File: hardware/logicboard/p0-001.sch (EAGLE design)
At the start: 31 parts, among them IC1 74ALS05N, IC2 LTC485N, IC3 LTC485N, J0 DC5V, J1 DIN5, J2 DIN5, J3 DIN5, X1 NELTRON-7810-XPXC, X2 NELTRON-7810-XPXC

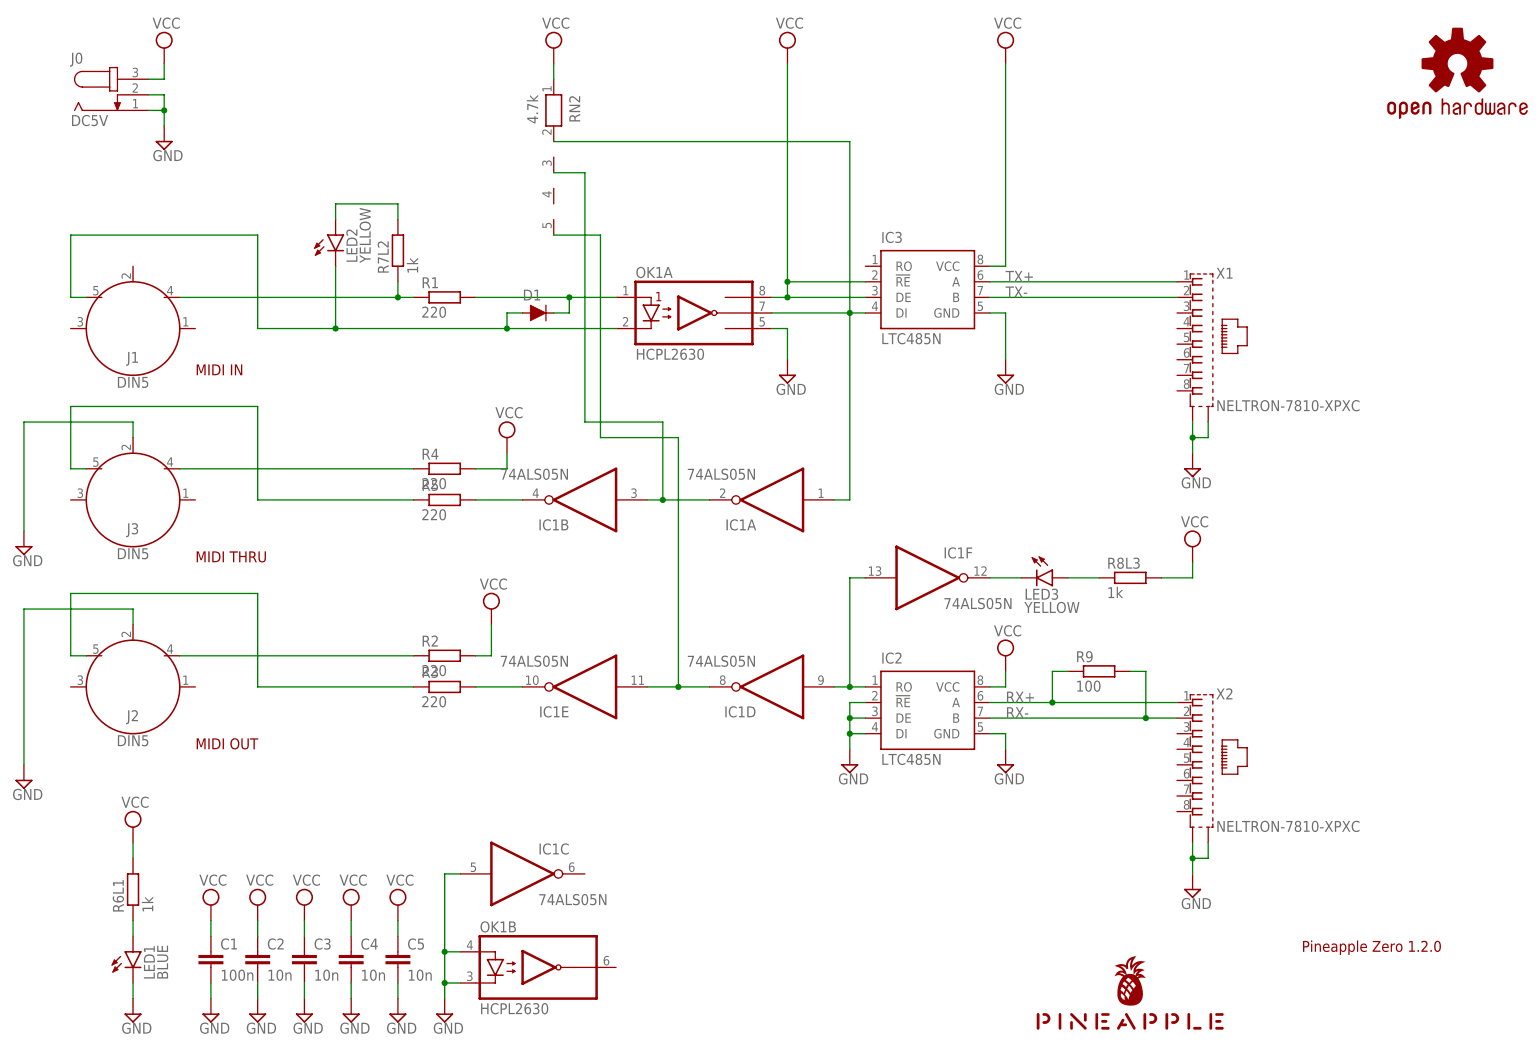
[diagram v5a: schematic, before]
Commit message: Changed led connection.
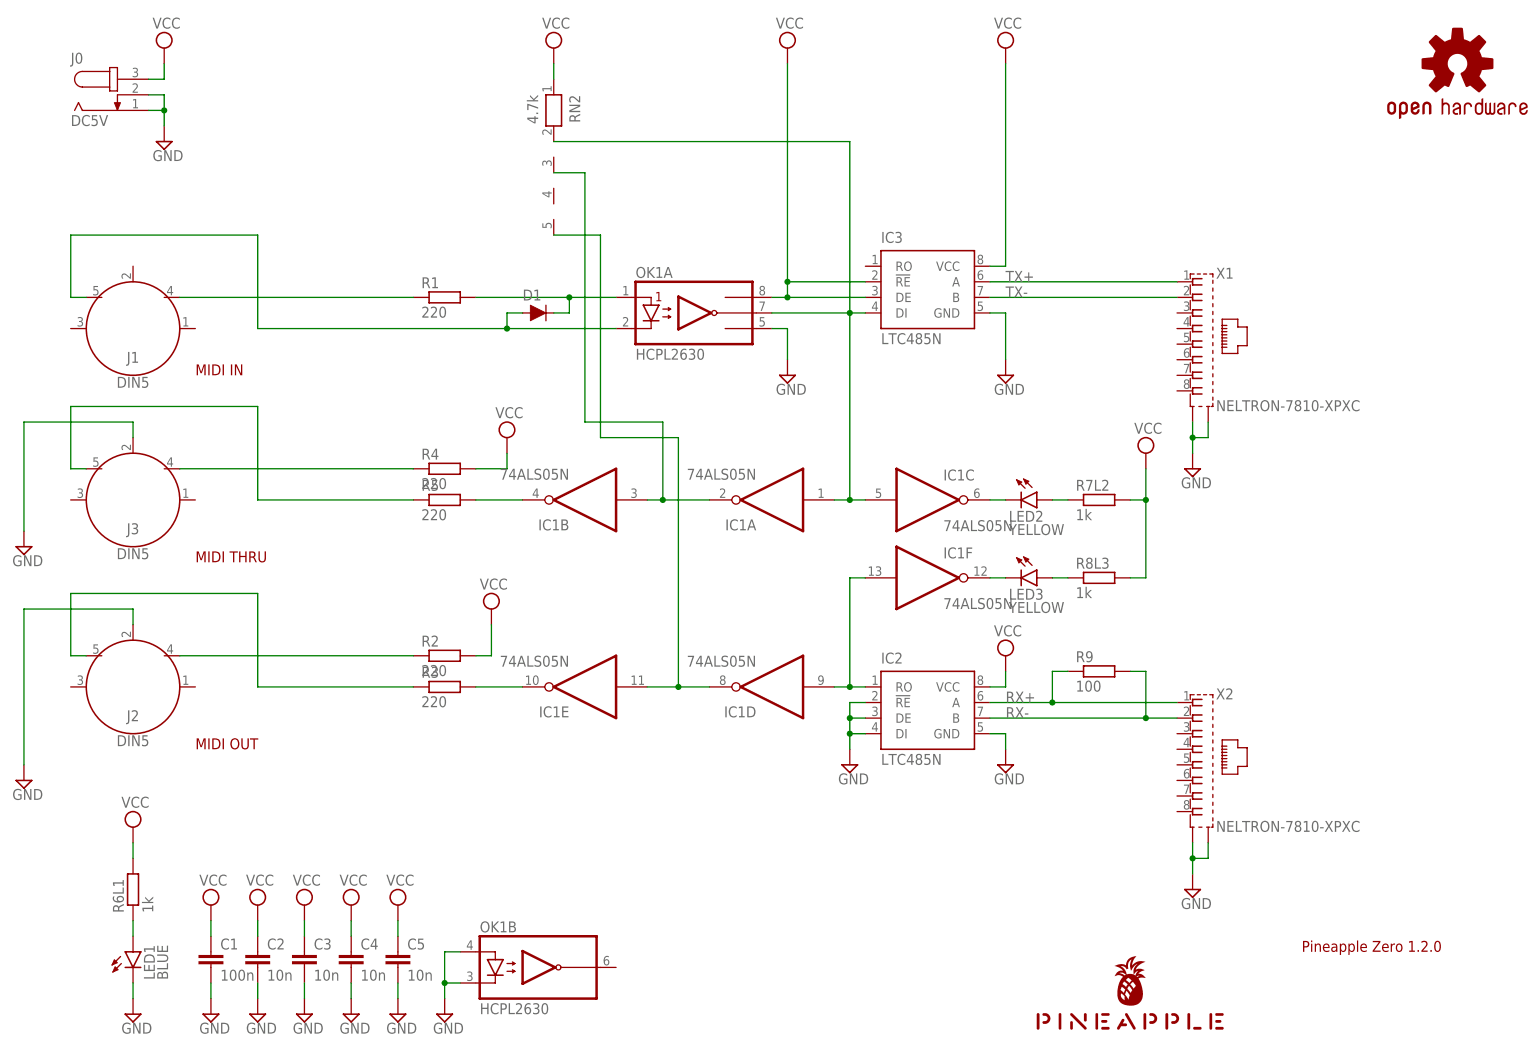
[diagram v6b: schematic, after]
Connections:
- new net N$5: LED2.A, R7L2.1
- net GND: no longer IC1C.I
- net MIRTN: no longer LED2.C
- net MISND: no longer R7L2.1
- net N$1: now also IC1C.O, LED2.C; no longer LED2.A, R7L2.2
- net TX: now also IC1C.I
- net VCC: now also R7L2.2
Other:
- moved on the sheet: IC1C, LED2, LED3, R7L2, R8L3
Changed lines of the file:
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@@
 <attribute name="VALUE" x="96.52" y="99.06" size="1.778" layer="96" rot="R180"/>
 </instance>
-<instance part="IC1" gate="C" x="88.9" y="33.02" smashed="yes">
-<attribute name="NAME" x="91.44" y="36.195" size="1.778" layer="95"/>
-<attribute name="VALUE" x="91.44" y="27.94" size="1.778" layer="96"/>
+<instance part="IC1" gate="C" x="154.94" y="93.98" smashed="yes">
+<attribute name="NAME" x="157.48" y="97.155" size="1.778" layer="95"/>
+<attribute name="VALUE" x="157.48" y="88.9" size="1.778" layer="96"/>
 </instance>
 <instance part="IC1" gate="D" x="129.54" y="63.5" smashed="yes" rot="R180">
@@
 <attribute name="VALUE" x="23.495" y="6.985" size="1.778" layer="96"/>
 </instance>
-<instance part="LED2" gate="G$1" x="58.42" y="137.16" smashed="yes">
-<attribute name="NAME" x="61.976" y="132.588" size="1.778" layer="95" rot="R90"/>
-<attribute name="VALUE" x="64.135" y="132.588" size="1.778" layer="96" rot="R90"/>
-</instance>
-<instance part="SUPPLY30" gate="G$1" x="198.12" y="86.36" smashed="yes">
-<attribute name="VALUE" x="196.215" y="89.535" size="1.778" layer="96"/>
-</instance>
-<instance part="LED3" gate="G$1" x="175.26" y="81.28" smashed="yes" rot="R270">
-<attribute name="NAME" x="170.688" y="77.724" size="1.778" layer="95"/>
-<attribute name="VALUE" x="170.688" y="75.565" size="1.778" layer="96"/>
+<instance part="LED2" gate="G$1" x="172.72" y="93.98" smashed="yes" rot="R270">
+<attribute name="NAME" x="168.148" y="90.424" size="1.778" layer="95"/>
+<attribute name="VALUE" x="168.148" y="88.265" size="1.778" layer="96"/>
+</instance>
+<instance part="SUPPLY30" gate="G$1" x="190.5" y="101.6" smashed="yes">
+<attribute name="VALUE" x="188.595" y="104.775" size="1.778" layer="96"/>
+</instance>
+<instance part="LED3" gate="G$1" x="172.72" y="81.28" smashed="yes" rot="R270">
+<attribute name="NAME" x="168.148" y="77.724" size="1.778" layer="95"/>
+<attribute name="VALUE" x="168.148" y="75.565" size="1.778" layer="96"/>
 </instance>
 <instance part="R9" gate="G$1" x="182.88" y="66.04" smashed="yes">
@@
 <attribute name="VALUE" x="72.39" y="60.198" size="1.778" layer="96"/>
 </instance>
-<instance part="R7L2" gate="G$1" x="68.58" y="134.62" smashed="yes" rot="R90">
-<attribute name="NAME" x="67.0814" y="130.81" size="1.778" layer="95" rot="R90"/>
-<attribute name="VALUE" x="71.882" y="130.81" size="1.778" layer="96" rot="R90"/>
-</instance>
-<instance part="R8L3" gate="G$1" x="187.96" y="81.28" smashed="yes">
-<attribute name="NAME" x="184.15" y="82.7786" size="1.778" layer="95"/>
-<attribute name="VALUE" x="184.15" y="77.978" size="1.778" layer="96"/>
+<instance part="R7L2" gate="G$1" x="182.88" y="93.98" smashed="yes">
+<attribute name="NAME" x="179.07" y="95.4786" size="1.778" layer="95"/>
+<attribute name="VALUE" x="179.07" y="90.678" size="1.778" layer="96"/>
+</instance>
+<instance part="R8L3" gate="G$1" x="182.88" y="81.28" smashed="yes">
+<attribute name="NAME" x="179.07" y="82.7786" size="1.778" layer="95"/>
+<attribute name="VALUE" x="179.07" y="77.978" size="1.778" layer="96"/>
 </instance>
 </instances>
@@
 <wire x1="78.74" y1="15.24" x2="76.2" y2="15.24" width="0.1524" layer="91"/>
 <junction x="76.2" y="15.24"/>
-<pinref part="IC1" gate="C" pin="I"/>
-<wire x1="78.74" y1="33.02" x2="76.2" y2="33.02" width="0.1524" layer="91"/>
-<wire x1="76.2" y1="33.02" x2="76.2" y2="20.32" width="0.1524" layer="91"/>
-<junction x="76.2" y="20.32"/>
 </segment>
 <segment>
@@
 <segment>
 <pinref part="SUPPLY30" gate="G$1" pin="VCC"/>
-<wire x1="198.12" y1="83.82" x2="198.12" y2="81.28" width="0.1524" layer="91"/>
+<wire x1="190.5" y1="99.06" x2="190.5" y2="93.98" width="0.1524" layer="91"/>
 <pinref part="R8L3" gate="G$1" pin="2"/>
-<wire x1="198.12" y1="81.28" x2="193.04" y2="81.28" width="0.1524" layer="91"/>
+<wire x1="190.5" y1="93.98" x2="190.5" y2="81.28" width="0.1524" layer="91"/>
+<wire x1="190.5" y1="81.28" x2="187.96" y2="81.28" width="0.1524" layer="91"/>
+<pinref part="R7L2" gate="G$1" pin="2"/>
+<wire x1="187.96" y1="93.98" x2="190.5" y2="93.98" width="0.1524" layer="91"/>
+<junction x="190.5" y="93.98"/>
 </segment>
 <segment>
@@
 <junction x="86.36" y="121.92"/>
 <pinref part="OK1" gate="A" pin="C1"/>
-<wire x1="45.72" y1="121.92" x2="58.42" y2="121.92" width="0.1524" layer="91"/>
-<pinref part="LED2" gate="G$1" pin="C"/>
-<wire x1="58.42" y1="121.92" x2="86.36" y2="121.92" width="0.1524" layer="91"/>
-<wire x1="58.42" y1="132.08" x2="58.42" y2="121.92" width="0.1524" layer="91"/>
-<junction x="58.42" y="121.92"/>
+<wire x1="45.72" y1="121.92" x2="86.36" y2="121.92" width="0.1524" layer="91"/>
 </segment>
 </net>
@@
 <wire x1="93.98" y1="152.4" x2="142.24" y2="152.4" width="0.1524" layer="91"/>
 <wire x1="142.24" y1="152.4" x2="142.24" y2="124.46" width="0.1524" layer="91"/>
+<pinref part="IC1" gate="C" pin="I"/>
+<wire x1="144.78" y1="93.98" x2="142.24" y2="93.98" width="0.1524" layer="91"/>
+<junction x="142.24" y="93.98"/>
 </segment>
 </net>
@@
 <pinref part="J1" gate="G$1" pin="4"/>
 <pinref part="R1" gate="G$1" pin="1"/>
-<wire x1="71.12" y1="127" x2="68.58" y2="127" width="0.1524" layer="91"/>
-<pinref part="R7L2" gate="G$1" pin="1"/>
-<wire x1="68.58" y1="127" x2="33.02" y2="127" width="0.1524" layer="91"/>
-<wire x1="68.58" y1="127" x2="68.58" y2="129.54" width="0.1524" layer="91"/>
-<junction x="68.58" y="127"/>
+<wire x1="71.12" y1="127" x2="33.02" y2="127" width="0.1524" layer="91"/>
 </segment>
 </net>
@@
 </segment>
 </net>
-<net name="N$1" class="0">
-<segment>
-<pinref part="R7L2" gate="G$1" pin="2"/>
-<wire x1="68.58" y1="139.7" x2="68.58" y2="142.24" width="0.1524" layer="91"/>
-<wire x1="68.58" y1="142.24" x2="58.42" y2="142.24" width="0.1524" layer="91"/>
-<pinref part="LED2" gate="G$1" pin="A"/>
-<wire x1="58.42" y1="142.24" x2="58.42" y2="139.7" width="0.1524" layer="91"/>
-</segment>
-</net>
 <net name="N$2" class="0">
 <segment>
 <pinref part="R8L3" gate="G$1" pin="1"/>
 <pinref part="LED3" gate="G$1" pin="A"/>
-<wire x1="182.88" y1="81.28" x2="177.8" y2="81.28" width="0.1524" layer="91"/>
+<wire x1="177.8" y1="81.28" x2="175.26" y2="81.28" width="0.1524" layer="91"/>
 </segment>
 </net>
@@
 <pinref part="LED3" gate="G$1" pin="C"/>
 <pinref part="IC1" gate="F" pin="O"/>
-<wire x1="170.18" y1="81.28" x2="165.1" y2="81.28" width="0.1524" layer="91"/>
+<wire x1="167.64" y1="81.28" x2="165.1" y2="81.28" width="0.1524" layer="91"/>
 </segment>
 </net>
@@
 </segment>
 </net>
+<net name="N$1" class="0">
+<segment>
+<pinref part="IC1" gate="C" pin="O"/>
+<pinref part="LED2" gate="G$1" pin="C"/>
+<wire x1="165.1" y1="93.98" x2="167.64" y2="93.98" width="0.1524" layer="91"/>
+</segment>
+</net>
+<net name="N$5" class="0">
+<segment>
+<pinref part="LED2" gate="G$1" pin="A"/>
+<pinref part="R7L2" gate="G$1" pin="1"/>
+<wire x1="175.26" y1="93.98" x2="177.8" y2="93.98" width="0.1524" layer="91"/>
+</segment>
+</net>

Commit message: Connector name.
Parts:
- renumbered J1 to J7, J2 to J9, J3 to J8, X1 to X9, X2 to X7
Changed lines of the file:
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@@
 <part name="LOGO1" library="SparkFun-Aesthetics" deviceset="OSHW-LOGO" device="S-COPPER" value="OSHW-LOGOS-COPPER"/>
 <part name="U$1" library="pineapple" deviceset="PINEAPPLE450" device=""/>
-<part name="J1" library="SparkFun-Connectors" library_urn="urn:adsk.eagle:library:513" deviceset="DIN5" device="" package3d_urn="urn:adsk.eagle:package:38294/1"/>
-<part name="J2" library="SparkFun-Connectors" library_urn="urn:adsk.eagle:library:513" deviceset="DIN5" device="" package3d_urn="urn:adsk.eagle:package:38294/1"/>
+<part name="J7" library="SparkFun-Connectors" library_urn="urn:adsk.eagle:library:513" deviceset="DIN5" device="" package3d_urn="urn:adsk.eagle:package:38294/1"/>
+<part name="J9" library="SparkFun-Connectors" library_urn="urn:adsk.eagle:library:513" deviceset="DIN5" device="" package3d_urn="urn:adsk.eagle:package:38294/1"/>
 <part name="J0" library="con-jack" library_urn="urn:adsk.eagle:library:154" deviceset="JACK-PLUG" device="0" package3d_urn="urn:adsk.eagle:package:7492/1" value="DC5V"/>
-<part name="J3" library="SparkFun-Connectors" library_urn="urn:adsk.eagle:library:513" deviceset="DIN5" device="" package3d_urn="urn:adsk.eagle:package:38294/1"/>
+<part name="J8" library="SparkFun-Connectors" library_urn="urn:adsk.eagle:library:513" deviceset="DIN5" device="" package3d_urn="urn:adsk.eagle:package:38294/1"/>
 <part name="SUPPLY1" library="supply2" library_urn="urn:adsk.eagle:library:372" deviceset="GND" device=""/>
 <part name="OK1" library="optocoupler" library_urn="urn:adsk.eagle:library:320" deviceset="HCPL2630" device="" package3d_urn="urn:adsk.eagle:package:21941/1"/>
@@
 <part name="LED3" library="led" library_urn="urn:adsk.eagle:library:259" deviceset="LED" device="3MM" package3d_urn="urn:adsk.eagle:package:15797/1" value="YELLOW"/>
 <part name="R9" library="rcl" library_urn="urn:adsk.eagle:library:334" deviceset="R-EU_" device="0204/5" package3d_urn="urn:adsk.eagle:package:23488/1" value="100"/>
-<part name="X1" library="con-rj45" deviceset="NELTRON-7810-XPXC" device=""/>
-<part name="X2" library="con-rj45" deviceset="NELTRON-7810-XPXC" device=""/>
+<part name="X9" library="con-rj45" deviceset="NELTRON-7810-XPXC" device=""/>
+<part name="X7" library="con-rj45" deviceset="NELTRON-7810-XPXC" device=""/>
 <part name="R6L1" library="rcl" library_urn="urn:adsk.eagle:library:334" deviceset="R-EU_" device="0204/5" package3d_urn="urn:adsk.eagle:package:23488/1" value="1k"/>
 <part name="R1" library="rcl" library_urn="urn:adsk.eagle:library:334" deviceset="R-EU_" device="0204/5" package3d_urn="urn:adsk.eagle:package:23488/1" value="220"/>
@@
 <instance part="LOGO1" gate="G$1" x="241.3" y="165.1" smashed="yes"/>
 <instance part="U$1" gate="G$1" x="187.96" y="7.62" smashed="yes"/>
-<instance part="J1" gate="G$1" x="25.4" y="121.92" smashed="yes">
+<instance part="J7" gate="G$1" x="25.4" y="121.92" smashed="yes">
 <attribute name="NAME" x="25.4" y="116.332" size="1.778" layer="95" font="vector" align="bottom-center"/>
 <attribute name="VALUE" x="25.4" y="114.046" size="1.778" layer="96" font="vector" align="top-center"/>
 </instance>
-<instance part="J2" gate="G$1" x="25.4" y="63.5" smashed="yes">
+<instance part="J9" gate="G$1" x="25.4" y="63.5" smashed="yes">
 <attribute name="NAME" x="25.4" y="57.912" size="1.778" layer="95" font="vector" align="bottom-center"/>
 <attribute name="VALUE" x="25.4" y="55.626" size="1.778" layer="96" font="vector" align="top-center"/>
@@
 <attribute name="VALUE" x="15.24" y="154.94" size="1.778" layer="96"/>
 </instance>
-<instance part="J3" gate="G$1" x="25.4" y="93.98" smashed="yes">
+<instance part="J8" gate="G$1" x="25.4" y="93.98" smashed="yes">
 <attribute name="NAME" x="25.4" y="88.392" size="1.778" layer="95" font="vector" align="bottom-center"/>
 <attribute name="VALUE" x="25.4" y="86.106" size="1.778" layer="96" font="vector" align="top-center"/>
@@
 <attribute name="VALUE" x="179.07" y="62.738" size="1.778" layer="96"/>
 </instance>
-<instance part="X1" gate="G$1" x="198.12" y="119.38" smashed="yes">
+<instance part="X9" gate="G$1" x="198.12" y="119.38" smashed="yes">
 <attribute name="NAME" x="201.93" y="130.048" size="1.778" layer="95"/>
 <attribute name="VALUE" x="201.93" y="108.458" size="1.778" layer="96"/>
 </instance>
-<instance part="X2" gate="G$1" x="198.12" y="50.8" smashed="yes">
+<instance part="X7" gate="G$1" x="198.12" y="50.8" smashed="yes">
 <attribute name="NAME" x="201.93" y="61.468" size="1.778" layer="95"/>
 <attribute name="VALUE" x="201.93" y="39.878" size="1.778" layer="96"/>
@@
 </segment>
 <segment>
-<pinref part="J3" gate="G$1" pin="2"/>
+<pinref part="J8" gate="G$1" pin="2"/>
 <wire x1="25.4" y1="104.14" x2="25.4" y2="106.68" width="0.1524" layer="91"/>
 <pinref part="SUPPLY22" gate="GND" pin="GND"/>
@@
 </segment>
 <segment>
-<pinref part="J2" gate="G$1" pin="2"/>
+<pinref part="J9" gate="G$1" pin="2"/>
 <wire x1="25.4" y1="73.66" x2="25.4" y2="76.2" width="0.1524" layer="91"/>
 <wire x1="25.4" y1="76.2" x2="7.62" y2="76.2" width="0.1524" layer="91"/>
@@
 <wire x1="198.12" y1="104.14" x2="198.12" y2="101.6" width="0.1524" layer="91"/>
 <junction x="198.12" y="104.14"/>
-<pinref part="X1" gate="G$1" pin="S2"/>
-<pinref part="X1" gate="G$1" pin="S1"/>
+<pinref part="X9" gate="G$1" pin="S2"/>
+<pinref part="X9" gate="G$1" pin="S1"/>
 </segment>
 <segment>
@@
 <wire x1="198.12" y1="35.56" x2="198.12" y2="33.02" width="0.1524" layer="91"/>
 <junction x="198.12" y="35.56"/>
-<pinref part="X2" gate="G$1" pin="S2"/>
-<pinref part="X2" gate="G$1" pin="S1"/>
+<pinref part="X7" gate="G$1" pin="S2"/>
+<pinref part="X7" gate="G$1" pin="S1"/>
 </segment>
 <segment>
@@
 <wire x1="165.1" y1="129.54" x2="195.58" y2="129.54" width="0.1524" layer="91"/>
 <label x="167.64" y="129.54" size="1.778" layer="95"/>
-<pinref part="X1" gate="G$1" pin="1"/>
+<pinref part="X9" gate="G$1" pin="1"/>
 </segment>
 </net>
@@
 <wire x1="86.36" y1="124.46" x2="88.9" y2="124.46" width="0.1524" layer="91"/>
 <wire x1="104.14" y1="121.92" x2="86.36" y2="121.92" width="0.1524" layer="91"/>
-<pinref part="J1" gate="G$1" pin="5"/>
+<pinref part="J7" gate="G$1" pin="5"/>
 <wire x1="17.78" y1="127" x2="15.24" y2="127" width="0.1524" layer="91"/>
 <wire x1="15.24" y1="127" x2="15.24" y2="137.16" width="0.1524" layer="91"/>
@@
 <wire x1="175.26" y1="66.04" x2="175.26" y2="60.96" width="0.1524" layer="91"/>
 <junction x="175.26" y="60.96"/>
-<pinref part="X2" gate="G$1" pin="1"/>
+<pinref part="X7" gate="G$1" pin="1"/>
 </segment>
 </net>
@@
 <wire x1="165.1" y1="127" x2="195.58" y2="127" width="0.1524" layer="91"/>
 <label x="167.64" y="127" size="1.778" layer="95"/>
-<pinref part="X1" gate="G$1" pin="2"/>
+<pinref part="X9" gate="G$1" pin="2"/>
 </segment>
 </net>
@@
 <wire x1="190.5" y1="66.04" x2="190.5" y2="58.42" width="0.1524" layer="91"/>
 <junction x="190.5" y="58.42"/>
-<pinref part="X2" gate="G$1" pin="2"/>
+<pinref part="X7" gate="G$1" pin="2"/>
 </segment>
 </net>
@@
 <net name="MTRTN" class="0">
 <segment>
-<pinref part="J3" gate="G$1" pin="5"/>
+<pinref part="J8" gate="G$1" pin="5"/>
 <wire x1="17.78" y1="99.06" x2="15.24" y2="99.06" width="0.1524" layer="91"/>
 <wire x1="15.24" y1="99.06" x2="15.24" y2="109.22" width="0.1524" layer="91"/>
@@
 <net name="MORTN" class="0">
 <segment>
-<pinref part="J2" gate="G$1" pin="5"/>
+<pinref part="J9" gate="G$1" pin="5"/>
 <wire x1="17.78" y1="68.58" x2="15.24" y2="68.58" width="0.1524" layer="91"/>
 <wire x1="15.24" y1="68.58" x2="15.24" y2="78.74" width="0.1524" layer="91"/>
@@
 <net name="MISND" class="0">
 <segment>
-<pinref part="J1" gate="G$1" pin="4"/>
+<pinref part="J7" gate="G$1" pin="4"/>
 <pinref part="R1" gate="G$1" pin="1"/>
 <wire x1="71.12" y1="127" x2="33.02" y2="127" width="0.1524" layer="91"/>
@@
 <net name="MOSND" class="0">
 <segment>
-<pinref part="J2" gate="G$1" pin="4"/>
+<pinref part="J9" gate="G$1" pin="4"/>
 <wire x1="71.12" y1="68.58" x2="33.02" y2="68.58" width="0.1524" layer="91"/>
 <pinref part="R2" gate="G$1" pin="1"/>
@@
 <net name="MTSND" class="0">
 <segment>
-<pinref part="J3" gate="G$1" pin="4"/>
+<pinref part="J8" gate="G$1" pin="4"/>
 <wire x1="71.12" y1="99.06" x2="33.02" y2="99.06" width="0.1524" layer="91"/>
 <pinref part="R4" gate="G$1" pin="1"/>
